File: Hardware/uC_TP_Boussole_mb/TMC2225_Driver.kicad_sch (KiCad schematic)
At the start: 13 parts, among them J2 Conn_01x04, U4 TMC2225-SA-T

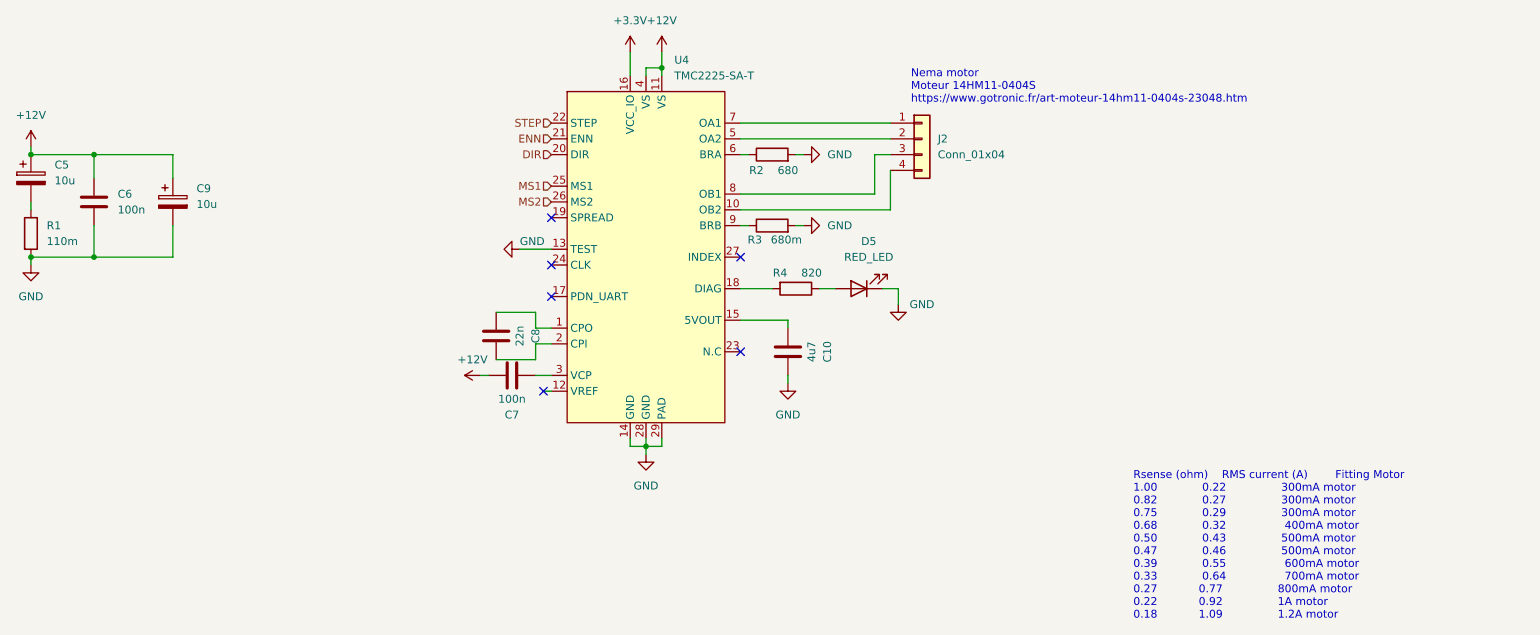
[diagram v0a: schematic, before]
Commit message: starting pin out nucleo
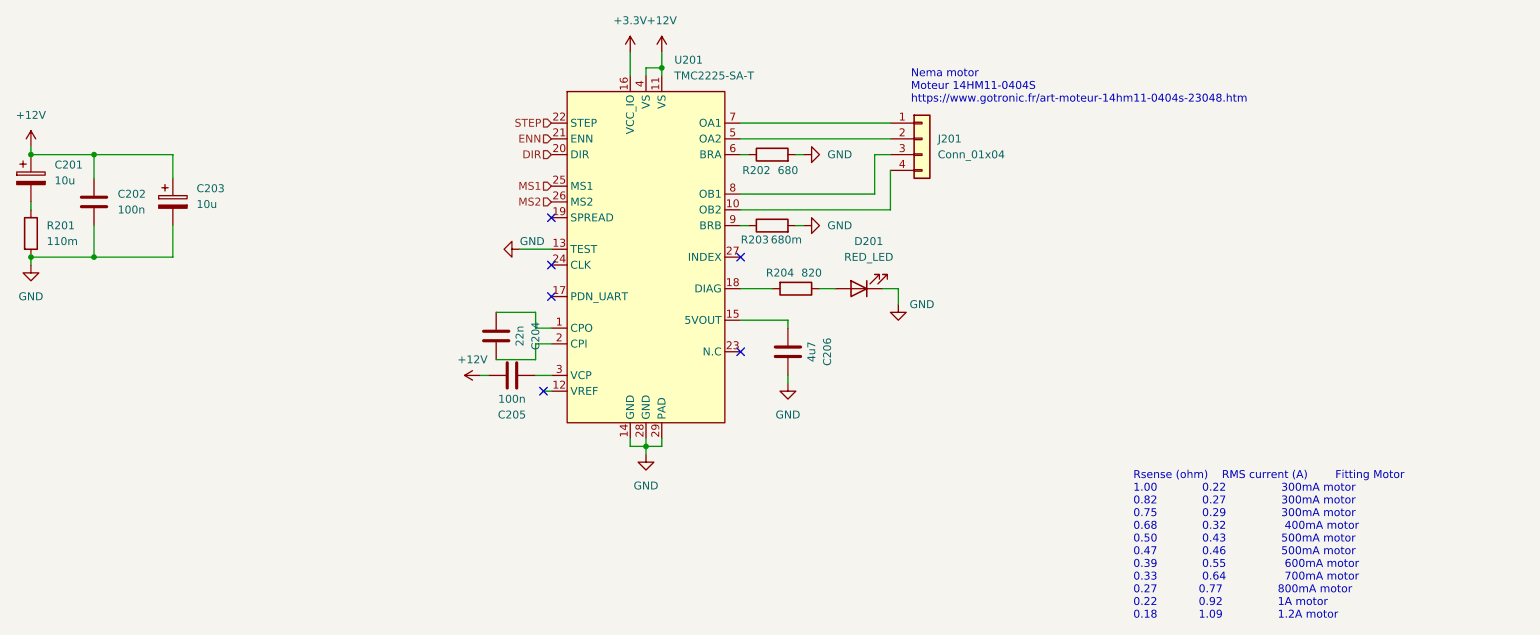
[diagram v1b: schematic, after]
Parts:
- C202: renamed from C6; footprint Capacitor_SMD:C_0603_1608Metric_Pad1.08x0.95mm_HandSolder -> Capacitor_SMD:C_0402_1005Metric
- C204: renamed from C8; footprint Capacitor_SMD:C_0603_1608Metric_Pad1.08x0.95mm_HandSolder -> Capacitor_SMD:C_0402_1005Metric
- C205: renamed from C7; footprint Capacitor_SMD:C_0603_1608Metric_Pad1.08x0.95mm_HandSolder -> Capacitor_SMD:C_0402_1005Metric
- C206: renamed from C10; footprint Capacitor_SMD:C_0805_2012Metric_Pad1.18x1.45mm_HandSolder -> Capacitor_SMD:C_0402_1005Metric
- D201: renamed from D5; footprint (none) -> LED_SMD:LED_0603_1608Metric
- J201: renamed from J2; footprint (none) -> Connector_JST:JST_XH_S4B-XH-A_1x04_P2.50mm_Horizontal
- renumbered C5 to C201, C9 to C203, R1 to R201, R2 to R202, R3 to R203, R4 to R204, U4 to U201
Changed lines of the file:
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@@
 		(dnp no)
 		(fields_autoplaced yes)
-		(property "Reference" "#PWR023"
+		(property "Reference" "#PWR0208"
 			(at 166.37 132.08 0)
 			(effects
@@
 			(project "uC_TP_Boussole_mb"
 				(path "/2e9feef3-d2ce-488a-99fa-e1de5099ffc3/3a7e115b-7ca3-45cc-80a9-3f3ed0217541"
-					(reference "#PWR023")
+					(reference "#PWR0208")
 					(unit 1)
 				)
@@
 		(dnp no)
 		(fields_autoplaced yes)
-		(property "Reference" "#PWR016"
+		(property "Reference" "#PWR0203"
 			(at 120.65 124.46 0)
 			(effects
@@
 			(project "uC_TP_Boussole_mb"
 				(path "/2e9feef3-d2ce-488a-99fa-e1de5099ffc3/3a7e115b-7ca3-45cc-80a9-3f3ed0217541"
-					(reference "#PWR016")
+					(reference "#PWR0203")
 					(unit 1)
 				)
@@
 		(on_board yes)
 		(dnp no)
-		(property "Reference" "R3"
+		(property "Reference" "R203"
 			(at 161.036 102.616 90)
 			(effects
@@
 			(project "uC_TP_Boussole_mb"
 				(path "/2e9feef3-d2ce-488a-99fa-e1de5099ffc3/3a7e115b-7ca3-45cc-80a9-3f3ed0217541"
-					(reference "R3")
+					(reference "R203")
 					(unit 1)
 				)
@@
 		(dnp no)
 		(fields_autoplaced yes)
-		(property "Reference" "D5"
+		(property "Reference" "D201"
 			(at 179.3875 102.87 0)
 			(effects
@@
 			)
 		)
-		(property "Footprint" ""
+		(property "Footprint" "LED_SMD:LED_0603_1608Metric"
 			(at 177.8 110.49 0)
 			(effects
@@
 			(project "uC_TP_Boussole_mb"
 				(path "/2e9feef3-d2ce-488a-99fa-e1de5099ffc3/3a7e115b-7ca3-45cc-80a9-3f3ed0217541"
-					(reference "D5")
+					(reference "D201")
 					(unit 1)
 				)
@@
 		(on_board yes)
 		(dnp no)
-		(property "Reference" "C7"
+		(property "Reference" "C205"
 			(at 121.92 130.81 90)
 			(effects
@@
 			)
 		)
-		(property "Footprint" "Capacitor_SMD:C_0603_1608Metric_Pad1.08x0.95mm_HandSolder"
+		(property "Footprint" "Capacitor_SMD:C_0402_1005Metric"
 			(at 125.73 123.4948 0)
 			(effects
@@
 			(project "uC_TP_Boussole_mb"
 				(path "/2e9feef3-d2ce-488a-99fa-e1de5099ffc3/3a7e115b-7ca3-45cc-80a9-3f3ed0217541"
-					(reference "C7")
+					(reference "C205")
 					(unit 1)
 				)
@@
 		(dnp no)
 		(fields_autoplaced yes)
-		(property "Reference" "J2"
+		(property "Reference" "J201"
 			(at 190.5 86.3599 0)
 			(effects
@@
 			)
 		)
-		(property "Footprint" ""
+		(property "Footprint" "Connector_JST:JST_XH_S4B-XH-A_1x04_P2.50mm_Horizontal"
 			(at 187.96 86.36 0)
 			(effects
@@
 			(project "uC_TP_Boussole_mb"
 				(path "/2e9feef3-d2ce-488a-99fa-e1de5099ffc3/3a7e115b-7ca3-45cc-80a9-3f3ed0217541"
-					(reference "J2")
+					(reference "J201")
 					(unit 1)
 				)
@@
 		(dnp no)
 		(fields_autoplaced yes)
-		(property "Reference" "C5"
+		(property "Reference" "C201"
 			(at 48.26 90.5509 0)
 			(effects
@@
 			(project "uC_TP_Boussole_mb"
 				(path "/2e9feef3-d2ce-488a-99fa-e1de5099ffc3/3a7e115b-7ca3-45cc-80a9-3f3ed0217541"
-					(reference "C5")
+					(reference "C201")
 					(unit 1)
 				)
@@
 		(dnp no)
 		(fields_autoplaced yes)
-		(property "Reference" "#PWR025"
+		(property "Reference" "#PWR0210"
 			(at 175.26 100.33 0)
 			(effects
@@
 			(project "uC_TP_Boussole_mb"
 				(path "/2e9feef3-d2ce-488a-99fa-e1de5099ffc3/3a7e115b-7ca3-45cc-80a9-3f3ed0217541"
-					(reference "#PWR025")
+					(reference "#PWR0210")
 					(unit 1)
 				)
@@
 		(on_board yes)
 		(dnp no)
-		(property "Reference" "#PWR018"
+		(property "Reference" "#PWR0204"
 			(at 116.84 104.14 0)
 			(effects
@@
 			(project "uC_TP_Boussole_mb"
 				(path "/2e9feef3-d2ce-488a-99fa-e1de5099ffc3/3a7e115b-7ca3-45cc-80a9-3f3ed0217541"
-					(reference "#PWR018")
+					(reference "#PWR0204")
 					(unit 1)
 				)
@@
 		(dnp no)
 		(fields_autoplaced yes)
-		(property "Reference" "C9"
+		(property "Reference" "C203"
 			(at 71.12 94.3609 0)
 			(effects
@@
 			(project "uC_TP_Boussole_mb"
 				(path "/2e9feef3-d2ce-488a-99fa-e1de5099ffc3/3a7e115b-7ca3-45cc-80a9-3f3ed0217541"
-					(reference "C9")
+					(reference "C203")
 					(unit 1)
 				)
@@
 		(on_board yes)
 		(dnp no)
-		(property "Reference" "C10"
+		(property "Reference" "C206"
 			(at 172.72 120.65 90)
 			(effects
@@
 			)
 		)
-		(property "Footprint" "Capacitor_SMD:C_0805_2012Metric_Pad1.18x1.45mm_HandSolder"
+		(property "Footprint" "Capacitor_SMD:C_0402_1005Metric"
 			(at 165.4048 116.84 0)
 			(effects
@@
 			(project "uC_TP_Boussole_mb"
 				(path "/2e9feef3-d2ce-488a-99fa-e1de5099ffc3/3a7e115b-7ca3-45cc-80a9-3f3ed0217541"
-					(reference "C10")
+					(reference "C206")
 					(unit 1)
 				)
@@
 		(on_board yes)
 		(dnp no)
-		(property "Reference" "C8"
+		(property "Reference" "C204"
 			(at 125.73 118.11 90)
 			(effects
@@
 			)
 		)
-		(property "Footprint" "Capacitor_SMD:C_0603_1608Metric_Pad1.08x0.95mm_HandSolder"
+		(property "Footprint" "Capacitor_SMD:C_0402_1005Metric"
 			(at 118.4148 114.3 0)
 			(effects
@@
 			(project "uC_TP_Boussole_mb"
 				(path "/2e9feef3-d2ce-488a-99fa-e1de5099ffc3/3a7e115b-7ca3-45cc-80a9-3f3ed0217541"
-					(reference "C8")
+					(reference "C204")
 					(unit 1)
 				)
@@
 		(on_board yes)
 		(dnp no)
-		(property "Reference" "R2"
+		(property "Reference" "R202"
 			(at 161.29 91.44 90)
 			(effects
@@
 			(project "uC_TP_Boussole_mb"
 				(path "/2e9feef3-d2ce-488a-99fa-e1de5099ffc3/3a7e115b-7ca3-45cc-80a9-3f3ed0217541"
-					(reference "R2")
+					(reference "R202")
 					(unit 1)
 				)
@@
 		(dnp no)
 		(fields_autoplaced yes)
-		(property "Reference" "#PWR024"
+		(property "Reference" "#PWR0209"
 			(at 175.26 88.9 0)
 			(effects
@@
 			(project "uC_TP_Boussole_mb"
 				(path "/2e9feef3-d2ce-488a-99fa-e1de5099ffc3/3a7e115b-7ca3-45cc-80a9-3f3ed0217541"
-					(reference "#PWR024")
+					(reference "#PWR0209")
 					(unit 1)
 				)
@@
 		(dnp no)
 		(fields_autoplaced yes)
-		(property "Reference" "U4"
+		(property "Reference" "U201"
 			(at 148.0694 73.66 0)
 			(effects
@@
 			(project "uC_TP_Boussole_mb"
 				(path "/2e9feef3-d2ce-488a-99fa-e1de5099ffc3/3a7e115b-7ca3-45cc-80a9-3f3ed0217541"
-					(reference "U4")
+					(reference "U201")
 					(unit 1)
 				)
@@
 		(dnp no)
 		(fields_autoplaced yes)
-		(property "Reference" "C6"
+		(property "Reference" "C202"
 			(at 58.42 95.2499 0)
 			(effects
@@
 			)
 		)
-		(property "Footprint" "Capacitor_SMD:C_0603_1608Metric_Pad1.08x0.95mm_HandSolder"
+		(property "Footprint" "Capacitor_SMD:C_0402_1005Metric"
 			(at 55.5752 100.33 0)
 			(effects
@@
 			(project "uC_TP_Boussole_mb"
 				(path "/2e9feef3-d2ce-488a-99fa-e1de5099ffc3/3a7e115b-7ca3-45cc-80a9-3f3ed0217541"
-					(reference "C6")
+					(reference "C202")
 					(unit 1)
 				)
@@
 		(dnp no)
 		(fields_autoplaced yes)
-		(property "Reference" "#PWR014"
+		(property "Reference" "#PWR0201"
 			(at 44.45 91.44 0)
 			(effects
@@
 			(project "uC_TP_Boussole_mb"
 				(path "/2e9feef3-d2ce-488a-99fa-e1de5099ffc3/3a7e115b-7ca3-45cc-80a9-3f3ed0217541"
-					(reference "#PWR014")
+					(reference "#PWR0201")
 					(unit 1)
 				)
@@
 		(on_board yes)
 		(dnp no)
-		(property "Reference" "R4"
+		(property "Reference" "R204"
 			(at 165.1 107.95 90)
 			(effects
@@
 			(project "uC_TP_Boussole_mb"
 				(path "/2e9feef3-d2ce-488a-99fa-e1de5099ffc3/3a7e115b-7ca3-45cc-80a9-3f3ed0217541"
-					(reference "R4")
+					(reference "R204")
 					(unit 1)
 				)
@@
 		(dnp no)
 		(fields_autoplaced yes)
-		(property "Reference" "#PWR022"
+		(property "Reference" "#PWR0207"
 			(at 146.05 76.2 0)
 			(effects
@@
 			(project "uC_TP_Boussole_mb"
 				(path "/2e9feef3-d2ce-488a-99fa-e1de5099ffc3/3a7e115b-7ca3-45cc-80a9-3f3ed0217541"
-					(reference "#PWR022")
+					(reference "#PWR0207")
 					(unit 1)
 				)
@@
 		(dnp no)
 		(fields_autoplaced yes)
-		(property "Reference" "#PWR020"
+		(property "Reference" "#PWR0205"
 			(at 140.97 76.2 0)
 			(effects
@@
 			(project "uC_TP_Boussole_mb"
 				(path "/2e9feef3-d2ce-488a-99fa-e1de5099ffc3/3a7e115b-7ca3-45cc-80a9-3f3ed0217541"
-					(reference "#PWR020")
+					(reference "#PWR0205")
 					(unit 1)
 				)
@@
 		(on_board yes)
 		(dnp no)
-		(property "Reference" "#PWR026"
+		(property "Reference" "#PWR0211"
 			(at 184.15 119.38 0)
 			(effects
@@
 			(project "uC_TP_Boussole_mb"
 				(path "/2e9feef3-d2ce-488a-99fa-e1de5099ffc3/3a7e115b-7ca3-45cc-80a9-3f3ed0217541"
-					(reference "#PWR026")
+					(reference "#PWR0211")
 					(unit 1)
 				)
@@
 		(dnp no)
 		(fields_autoplaced yes)
-		(property "Reference" "#PWR021"
+		(property "Reference" "#PWR0206"
 			(at 143.51 143.51 0)
 			(effects
@@
 			(project "uC_TP_Boussole_mb"
 				(path "/2e9feef3-d2ce-488a-99fa-e1de5099ffc3/3a7e115b-7ca3-45cc-80a9-3f3ed0217541"
-					(reference "#PWR021")
+					(reference "#PWR0206")
 					(unit 1)
 				)
@@
 		(dnp no)
 		(fields_autoplaced yes)
-		(property "Reference" "#PWR015"
+		(property "Reference" "#PWR0202"
 			(at 44.45 113.03 0)
 			(effects
@@
 			(project "uC_TP_Boussole_mb"
 				(path "/2e9feef3-d2ce-488a-99fa-e1de5099ffc3/3a7e115b-7ca3-45cc-80a9-3f3ed0217541"
-					(reference "#PWR015")
+					(reference "#PWR0202")
 					(unit 1)
 				)
@@
 		(dnp no)
 		(fields_autoplaced yes)
-		(property "Reference" "R1"
+		(property "Reference" "R201"
 			(at 46.99 100.3299 0)
 			(effects
@@
 			(project "uC_TP_Boussole_mb"
 				(path "/2e9feef3-d2ce-488a-99fa-e1de5099ffc3/3a7e115b-7ca3-45cc-80a9-3f3ed0217541"
-					(reference "R1")
-					(unit 1)
-				)
+					(reference "R201")
+					(unit 1)
+				)

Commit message: update pcb
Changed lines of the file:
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@@
 		)
 		(property "Value" "680m"
-			(at 166.116 102.616 90)
+			(at 166.878 102.616 90)
 			(effects
 				(font

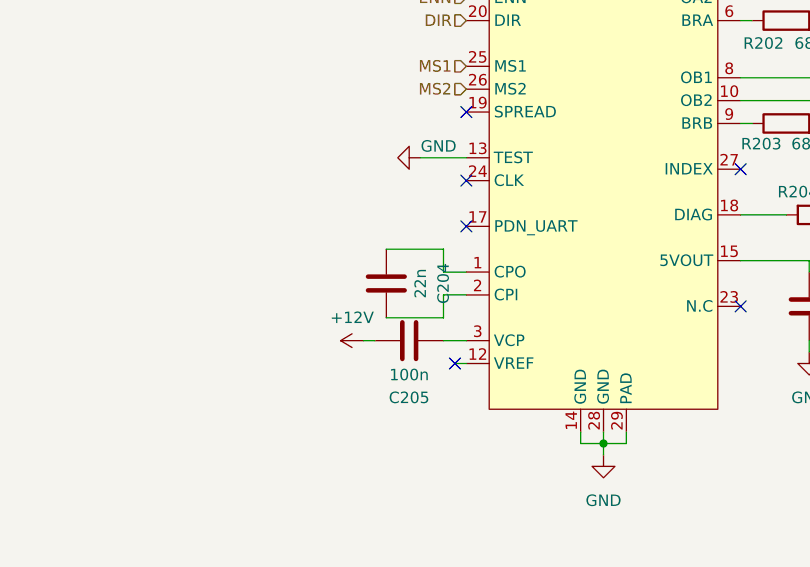
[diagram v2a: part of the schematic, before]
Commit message: update schematic
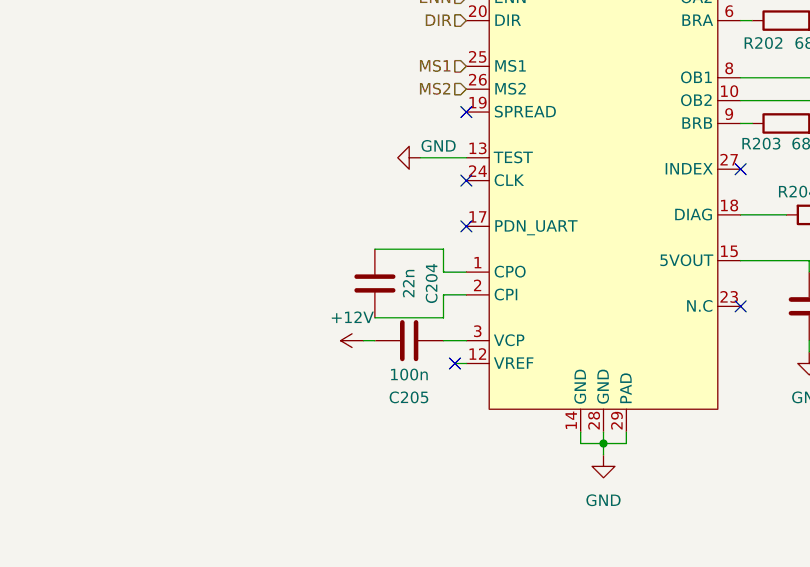
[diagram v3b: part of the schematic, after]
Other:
- moved on the sheet: C204
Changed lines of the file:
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@@
 	(wire
 		(pts
-			(xy 119.38 114.3) (xy 125.73 114.3)
+			(xy 118.11 114.3) (xy 125.73 114.3)
 		)
 		(stroke
@@
 	(wire
 		(pts
-			(xy 119.38 121.92) (xy 125.73 121.92)
+			(xy 118.11 121.92) (xy 125.73 121.92)
 		)
 		(stroke
@@
 	(symbol
 		(lib_id "Device:C")
-		(at 119.38 118.11 180)
+		(at 118.11 118.11 180)
 		(unit 1)
 		(exclude_from_sim no)
@@
 		(dnp no)
 		(property "Reference" "C204"
-			(at 125.73 118.11 90)
+			(at 124.46 118.11 90)
 			(effects
 				(font
@@
 		)
 		(property "Value" "22n"
-			(at 123.19 118.11 90)
+			(at 121.92 118.11 90)
 			(effects
 				(font
@@
 		)
 		(property "Footprint" "Capacitor_SMD:C_0402_1005Metric"
-			(at 118.4148 114.3 0)
+			(at 117.1448 114.3 0)
 			(effects
 				(font
@@
 		)
 		(property "Datasheet" "~"
-			(at 119.38 118.11 0)
+			(at 118.11 118.11 0)
 			(effects
 				(font
@@
 		)
 		(property "Description" ""
-			(at 119.38 118.11 0)
+			(at 118.11 118.11 0)
 			(effects
 				(font
@@
 		)
 		(property "Vmax" "50V"
-			(at 119.38 118.11 90)
-			(effects
-				(font
+			(at 118.11 118.11 90)
+			(effects
+				(font

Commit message: ddd
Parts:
- R202: value 680 -> 680m
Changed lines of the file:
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@@
 			)
 		)
-		(property "Value" "680"
+		(property "Value" "680m"
 			(at 166.37 91.44 90)
 			(effects

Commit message: finalize pcb
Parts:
- R204: footprint Resistor_SMD:R_0603_1608Metric_Pad0.98x0.95mm_HandSolder -> Resistor_SMD:R_0402_1005Metric
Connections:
- net A1: now reaches U201.7 (OA1)
- net A1: now also J201.3 (Pin_3); no longer J201.1 (Pin_1)
- net A2: now reaches U201.5 (OA2)
- net A2: now also J201.4 (Pin_4); no longer J201.2 (Pin_2)
- net B1: now reaches U201.8 (OB1)
- net B1: now also J201.2 (Pin_2); no longer J201.3 (Pin_3)
- net B2: now reaches U201.10 (OB2)
- net B2: now also J201.1 (Pin_1); no longer J201.4 (Pin_4)
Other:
- moved on the sheet: J201
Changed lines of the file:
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@@
 	(wire
 		(pts
-			(xy 180.34 95.25) (xy 180.34 88.9)
+			(xy 158.75 86.36) (xy 163.83 86.36)
 		)
 		(stroke
@@
 	(wire
 		(pts
-			(xy 158.75 86.36) (xy 182.88 86.36)
-		)
-		(stroke
-			(width 0)
-			(type default)
-		)
-	)
-	(wire
-		(pts
 			(xy 143.51 76.2) (xy 143.51 74.93)
 		)
@@
 	(wire
 		(pts
+			(xy 158.75 97.79) (xy 163.83 97.79)
+		)
+		(stroke
+			(width 0)
+			(type default)
+		)
+	)
+	(wire
+		(pts
 			(xy 184.15 110.49) (xy 181.61 110.49)
 		)
@@
 	(wire
 		(pts
+			(xy 179.07 95.25) (xy 184.15 95.25)
+		)
+		(stroke
+			(width 0)
+			(type default)
+		)
+	)
+	(wire
+		(pts
 			(xy 44.45 96.52) (xy 44.45 97.79)
 		)
@@
 	(wire
 		(pts
-			(xy 182.88 97.79) (xy 182.88 91.44)
+			(xy 158.75 83.82) (xy 163.83 83.82)
 		)
 		(stroke
@@
 	(wire
 		(pts
-			(xy 158.75 83.82) (xy 182.88 83.82)
-		)
-		(stroke
-			(width 0)
-			(type default)
-		)
-	)
-	(wire
-		(pts
 			(xy 54.61 88.9) (xy 67.31 88.9)
 		)
@@
 	(wire
 		(pts
+			(xy 179.07 87.63) (xy 184.15 87.63)
+		)
+		(stroke
+			(width 0)
+			(type default)
+		)
+	)
+	(wire
+		(pts
 			(xy 146.05 72.39) (xy 146.05 74.93)
 		)
@@
 	(wire
 		(pts
-			(xy 180.34 88.9) (xy 182.88 88.9)
+			(xy 179.07 92.71) (xy 184.15 92.71)
 		)
 		(stroke
@@
 	(wire
 		(pts
-			(xy 158.75 97.79) (xy 182.88 97.79)
-		)
-		(stroke
-			(width 0)
-			(type default)
-		)
-	)
-	(wire
-		(pts
 			(xy 158.75 115.57) (xy 166.37 115.57)
 		)
@@
 	(wire
 		(pts
-			(xy 158.75 95.25) (xy 180.34 95.25)
+			(xy 158.75 95.25) (xy 163.83 95.25)
 		)
 		(stroke
@@
 		(pts
 			(xy 125.73 114.3) (xy 125.73 116.84)
+		)
+		(stroke
+			(width 0)
+			(type default)
+		)
+	)
+	(wire
+		(pts
+			(xy 179.07 90.17) (xy 184.15 90.17)
 		)
 		(stroke
@@
 			)
 			(justify left)
+		)
+	)
+	(label "B2"
+		(at 179.07 87.63 0)
+		(fields_autoplaced yes)
+		(effects
+			(font
+				(size 1.27 1.27)
+			)
+			(justify left bottom)
+		)
+	)
+	(label "B1"
+		(at 179.07 90.17 0)
+		(fields_autoplaced yes)
+		(effects
+			(font
+				(size 1.27 1.27)
+			)
+			(justify left bottom)
+		)
+	)
+	(label "A2"
+		(at 163.83 86.36 180)
+		(fields_autoplaced yes)
+		(effects
+			(font
+				(size 1.27 1.27)
+			)
+			(justify right bottom)
+		)
+	)
+	(label "A1"
+		(at 179.07 92.71 0)
+		(fields_autoplaced yes)
+		(effects
+			(font
+				(size 1.27 1.27)
+			)
+			(justify left bottom)
+		)
+	)
+	(label "A2"
+		(at 179.07 95.25 0)
+		(fields_autoplaced yes)
+		(effects
+			(font
+				(size 1.27 1.27)
+			)
+			(justify left bottom)
+		)
+	)
+	(label "B1"
+		(at 163.83 95.25 180)
+		(fields_autoplaced yes)
+		(effects
+			(font
+				(size 1.27 1.27)
+			)
+			(justify right bottom)
+		)
+	)
+	(label "B2"
+		(at 163.83 97.79 180)
+		(fields_autoplaced yes)
+		(effects
+			(font
+				(size 1.27 1.27)
+			)
+			(justify right bottom)
+		)
+	)
+	(label "A1"
+		(at 163.83 83.82 180)
+		(fields_autoplaced yes)
+		(effects
+			(font
+				(size 1.27 1.27)
+			)
+			(justify right bottom)
 		)
 	)
@@
 	(symbol
 		(lib_id "Connector_Generic:Conn_01x04")
-		(at 187.96 86.36 0)
+		(at 189.23 90.17 0)
 		(unit 1)
 		(exclude_from_sim no)
@@
 		(fields_autoplaced yes)
 		(property "Reference" "J201"
-			(at 190.5 86.3599 0)
+			(at 191.77 90.1699 0)
 			(effects
 				(font
@@
 		)
 		(property "Value" "Conn_01x04"
-			(at 190.5 88.8999 0)
+			(at 191.77 92.7099 0)
 			(effects
 				(font
@@
 		)
 		(property "Footprint" "Connector_JST:JST_XH_S4B-XH-A_1x04_P2.50mm_Horizontal"
-			(at 187.96 86.36 0)
+			(at 189.23 90.17 0)
 			(effects
 				(font
@@
 		)
 		(property "Datasheet" "~"
-			(at 187.96 86.36 0)
+			(at 189.23 90.17 0)
 			(effects
 				(font
@@
 		)
 		(property "Description" "Generic connector, single row, 01x04, script generated (kicad-library-utils/schlib/autogen/connector/)"
-			(at 187.96 86.36 0)
+			(at 189.23 90.17 0)
 			(effects
 				(font
@@
 			)
 		)
-		(property "Footprint" "Resistor_SMD:R_0603_1608Metric_Pad0.98x0.95mm_HandSolder"
+		(property "Footprint" "Resistor_SMD:R_0402_1005Metric"
 			(at 167.64 108.712 90)
 			(effects

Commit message: bom
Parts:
- D201: MPN 150060RS55040 -> WE 150060RS55040
- R201: MPN (none) -> MFL0603R1100FB
- R202, R203: MPN (none) -> WW12PR680FTL
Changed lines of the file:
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@@
+			)
+		)
+		(property "MPN" "WW12PR680FTL "
+			(at 163.83 100.33 0)
+			(effects
+				(font
+					(size 1.27 1.27)
+				)
+				(hide yes)
 			)
 		)
@@
 			)
 		)
-		(property "MPN" "150060RS55040"
+		(property "MPN" "WE 150060RS55040"
 			(at 177.8 110.49 90)
 			(effects
@@
 			)
 		)
+		(property "MPN" "WW12PR680FTL "
+			(at 163.83 88.9 0)
+			(effects
+				(font
+					(size 1.27 1.27)
+				)
+				(hide yes)
+			)
+		)
 		(pin "1"
 		)
@@
 			(at 44.45 101.6 0)
 			(effects
+				(font
+					(size 1.27 1.27)
+				)
+				(hide yes)
+			)
+		)
+		(property "MPN" "MFL0603R1100FB "
+			(at 44.45 101.6 0)
+			(effects
